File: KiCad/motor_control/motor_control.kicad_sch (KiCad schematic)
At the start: 5 parts

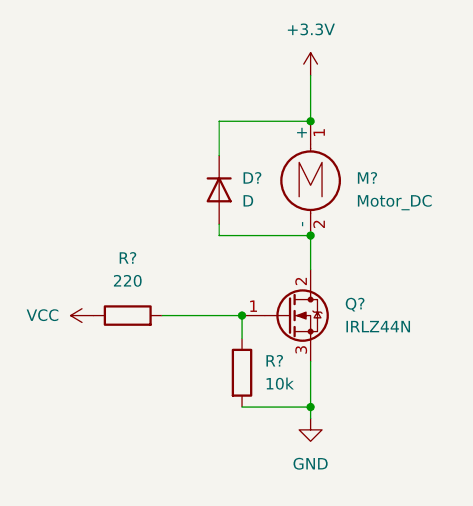
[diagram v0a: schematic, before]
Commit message: HC-05 finally works!!!!
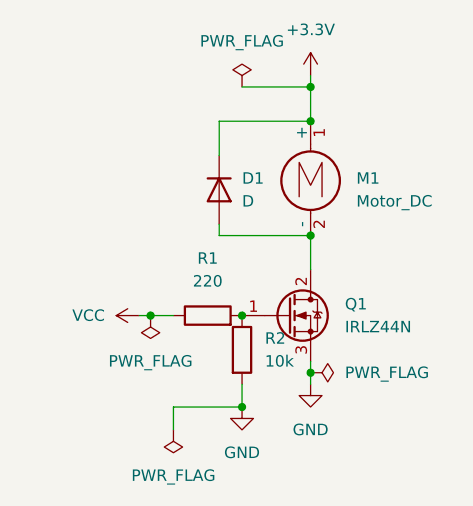
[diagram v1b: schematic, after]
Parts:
- gave numbers to parts that had none: 5
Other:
- moved on the sheet: R1, R2
